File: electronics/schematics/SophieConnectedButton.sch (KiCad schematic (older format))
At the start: 13 parts, among them SW1 BT1, SW2 BT2, SW3 BT3, SW4 BT4

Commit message: Version semiminiature. Fin de journée 14octo2016
Inversion des serials 1 et 2
Modification de la patte Reset du module
Alignement de toutes les variables
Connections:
- wire segments 49 -> 52
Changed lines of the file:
@@
 	8050 3350 8050 3500
 Wire Wire Line
-	9300 2450 9300 3950
+	9300 2450 9300 4100
 Wire Wire Line
 	9300 3200 9050 3200
-Wire Wire Line
-	9300 3950 7850 3950
 Wire Wire Line
 	5950 3500 6050 3500
 Wire Wire Line
 	6050 3650 6200 3650
-Wire Wire Line
-	5950 3800 6200 3800
 Wire Wire Line
 	6050 3500 6050 3650
@@
 	1    0    0    -1
 $EndComp
-Wire Wire Line
-	5350 3250 5350 3800
 $Comp
 L +3.3V #PWR?
@@
 Wire Wire Line
 	8650 3500 8650 3650
-Wire Wire Line
-	8650 3650 8850 3650
 Wire Wire Line
 	4000 1950 4400 1950
@@
 $EndComp
 Wire Wire Line
-	6200 3350 6100 3350
-Wire Wire Line
-	6100 3350 6100 1500
-Wire Wire Line
-	6100 1500 2400 1500
-Wire Wire Line
 	2400 1500 2400 2050
 Wire Wire Line
@@
 Wire Wire Line
 	4900 2850 4900 3000
+Wire Wire Line
+	9300 4100 7850 4100
+Connection ~ 7850 4100
+Wire Wire Line
+	8850 3950 7950 3950
+Wire Wire Line
+	5350 3250 5350 3800
+Connection ~ 5350 3250
+Connection ~ 3400 2200
+Wire Wire Line
+	7950 3950 7950 3800
+Wire Wire Line
+	7950 3800 7850 3800
+Wire Wire Line
+	7850 3500 7950 3500
+Wire Wire Line
+	2400 1500 7950 1500
+Wire Wire Line
+	7950 1500 7950 3500
+Connection ~ 5350 3500
+Wire Wire Line
+	6200 3800 5950 3800
+Wire Wire Line
+	7850 3650 8850 3650
+Connection ~ 8650 3650
 $EndSCHEMATC

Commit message: Tests intermediaires
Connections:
- net labels added: +BATT
- wire segments 52 -> 53
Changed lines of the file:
@@
 	1    0    0    -1
 $EndComp
-Wire Wire Line
-	4000 4250 4000 4400
-Wire Wire Line
-	7850 3950 7850 4150
 $Comp
 L SW_PUSH SW3
@@
 	1    0    0    -1
 $EndComp
-Wire Wire Line
-	7850 3200 8150 3200
-Wire Wire Line
-	8450 3200 8650 3200
-Wire Wire Line
-	7850 3350 8050 3350
-Wire Wire Line
-	8050 3350 8050 3500
-Wire Wire Line
-	9300 2450 9300 4100
-Wire Wire Line
-	9300 3200 9050 3200
-Wire Wire Line
-	5950 3500 6050 3500
-Wire Wire Line
-	6050 3650 6200 3650
-Wire Wire Line
-	6050 3500 6050 3650
-Wire Wire Line
-	5950 3250 6150 3250
-Wire Wire Line
-	6150 3250 6150 3500
-Wire Wire Line
-	6150 3500 6200 3500
-Wire Wire Line
-	5900 2850 6000 2850
-Wire Wire Line
-	6000 2850 6000 3200
-Wire Wire Line
-	6000 3200 6200 3200
-Wire Wire Line
-	5400 2850 5600 2850
 $Comp
 L +3.3V #PWR?
@@
 	1    0    0    -1
 $EndComp
-Wire Wire Line
-	8650 3500 8650 3650
-Wire Wire Line
-	4000 1950 4400 1950
-Wire Wire Line
-	4400 1850 4400 2000
-Wire Wire Line
-	4400 1850 4000 1850
 $Comp
 L GND #PWR?
@@
 	1    0    0    -1
 $EndComp
-Wire Wire Line
-	7850 3050 8700 3050
-Wire Wire Line
-	8700 3050 8700 2900
-Wire Wire Line
-	7850 2900 8450 2900
-Wire Wire Line
-	8450 2900 8450 2800
-Wire Wire Line
-	8450 2800 8700 2800
-Wire Wire Line
-	8700 2700 8700 2450
-Wire Wire Line
-	8700 2450 9300 2450
-Connection ~ 9300 3200
 $Comp
 L GND #PWR?
@@
 	1    0    0    -1
 $EndComp
-Wire Wire Line
-	2400 1500 2400 2050
-Wire Wire Line
-	6650 2250 6650 1950
-Wire Wire Line
-	6650 1950 4900 1950
-Wire Wire Line
-	4900 1950 4900 2550
-Wire Wire Line
-	4900 2550 4000 2550
-Wire Wire Line
-	2400 2550 2300 2550
-Wire Wire Line
-	2300 2550 2300 1400
-Wire Wire Line
-	2300 1400 6800 1400
-Wire Wire Line
-	6800 1400 6800 2250
 $Comp
 L CONN_01X02 P?
@@
 	-1   0    0    -1
 $EndComp
+$Comp
+L +3.3V #PWR?
+U 1 1 580109B9
+P 4400 1750
+F 0 "#PWR?" H 4400 1600 50  0001 C CNN
+F 1 "+3.3V" H 4400 1890 50  0000 C CNN
+F 2 "" H 4400 1750 50  0000 C CNN
+F 3 "" H 4400 1750 50  0000 C CNN
+	1    4400 1750
+	1    0    0    -1
+$EndComp
+Wire Wire Line
+	4000 4250 4000 4400
+Wire Wire Line
+	7850 3950 7850 4150
+Wire Wire Line
+	7850 3200 8150 3200
+Wire Wire Line
+	8450 3200 8650 3200
+Wire Wire Line
+	7850 3350 8050 3350
+Wire Wire Line
+	8050 3350 8050 3500
+Wire Wire Line
+	9300 2450 9300 4100
+Wire Wire Line
+	9300 3200 9050 3200
+Wire Wire Line
+	5950 3500 6050 3500
+Wire Wire Line
+	6050 3650 6200 3650
+Wire Wire Line
+	6050 3500 6050 3650
+Wire Wire Line
+	5950 3250 6150 3250
+Wire Wire Line
+	6150 3250 6150 3500
+Wire Wire Line
+	6150 3500 6200 3500
+Wire Wire Line
+	5900 2850 6000 2850
+Wire Wire Line
+	6000 2850 6000 3200
+Wire Wire Line
+	6000 3200 6200 3200
+Wire Wire Line
+	5400 2850 5600 2850
+Wire Wire Line
+	8650 3500 8650 3650
+Wire Wire Line
+	4000 1950 4400 1950
+Wire Wire Line
+	4400 1750 4400 2000
+Wire Wire Line
+	4400 1850 4000 1850
+Wire Wire Line
+	7850 3050 8700 3050
+Wire Wire Line
+	8700 3050 8700 2900
+Wire Wire Line
+	7850 2900 8450 2900
+Wire Wire Line
+	8450 2900 8450 2800
+Wire Wire Line
+	8450 2800 8700 2800
+Wire Wire Line
+	8700 2700 8700 2450
+Wire Wire Line
+	8700 2450 9300 2450
+Connection ~ 9300 3200
+Wire Wire Line
+	2400 1500 2400 2050
+Wire Wire Line
+	6650 2250 6650 1950
+Wire Wire Line
+	6650 1950 4900 1950
+Wire Wire Line
+	4900 1950 4900 2550
+Wire Wire Line
+	4900 2550 4000 2550
+Wire Wire Line
+	2400 2550 2300 2550
+Wire Wire Line
+	2300 2550 2300 1400
+Wire Wire Line
+	2300 1400 6800 1400
+Wire Wire Line
+	6800 1400 6800 2250
 Wire Wire Line
 	2050 2150 2400 2150
@@
 Connection ~ 7850 4100
 Wire Wire Line
-	8850 3950 7950 3950
+	7950 3950 9050 3950
 Wire Wire Line
 	5350 3250 5350 3800
 Connection ~ 5350 3250
-Connection ~ 3400 2200
 Wire Wire Line
 	7950 3950 7950 3800
@@
 	7850 3650 8850 3650
 Connection ~ 8650 3650
+Connection ~ 4400 1850
+Connection ~ 4400 1950
+$Comp
+L +BATT #PWR?
+U 1 1 580117AC
+P 9050 3850
+F 0 "#PWR?" H 9050 3700 50  0001 C CNN
+F 1 "+BATT" H 9050 3990 50  0000 C CNN
+F 2 "" H 9050 3850 50  0000 C CNN
+F 3 "" H 9050 3850 50  0000 C CNN
+	1    9050 3850
+	1    0    0    -1
+$EndComp
+Wire Wire Line
+	9050 3950 9050 3850
 $EndSCHEMATC

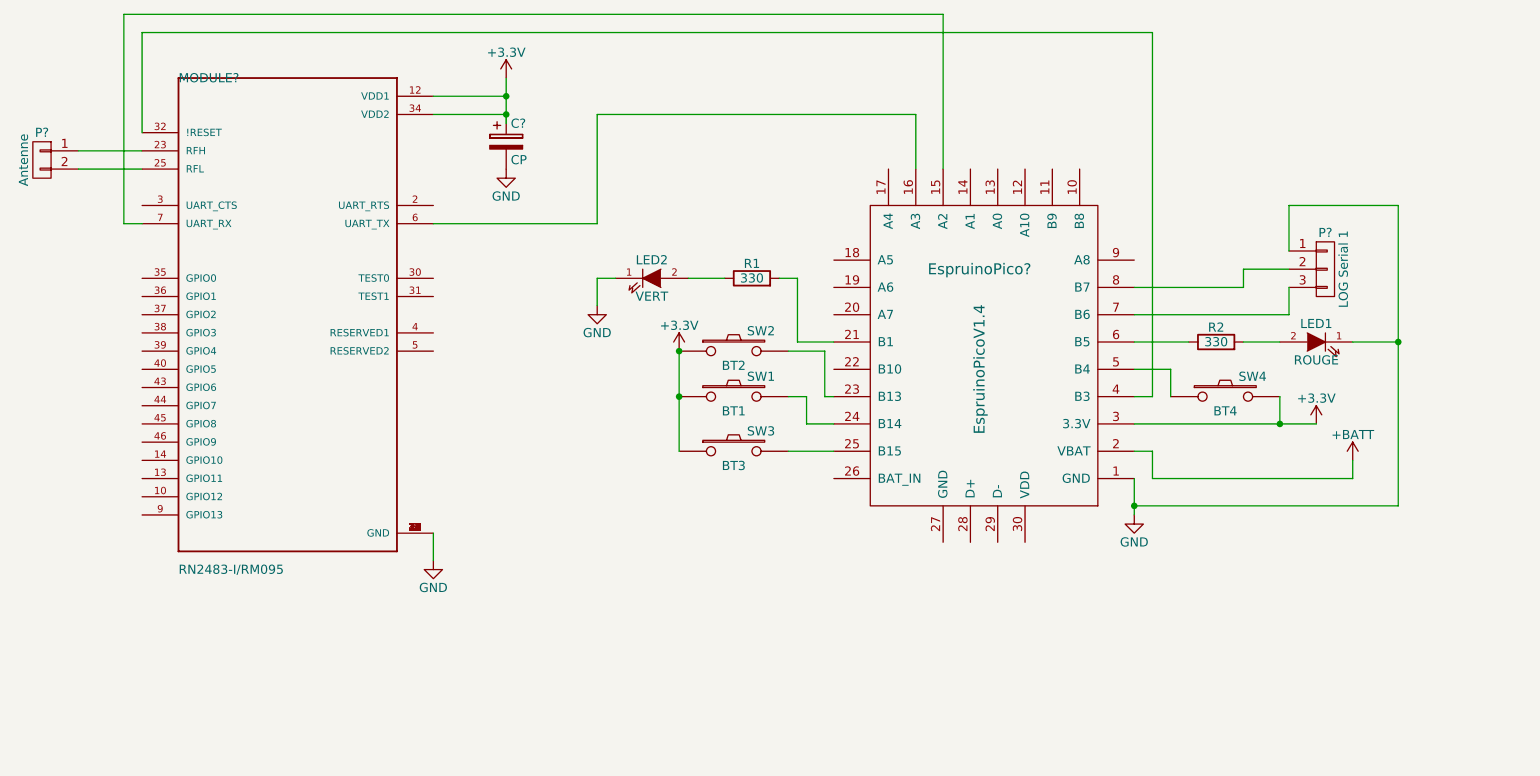
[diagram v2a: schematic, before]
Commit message: Forçage de la console sur USB
Correction forçant la console sur l'USB, ne polluant plus Serial1.
Divers nettoyages.
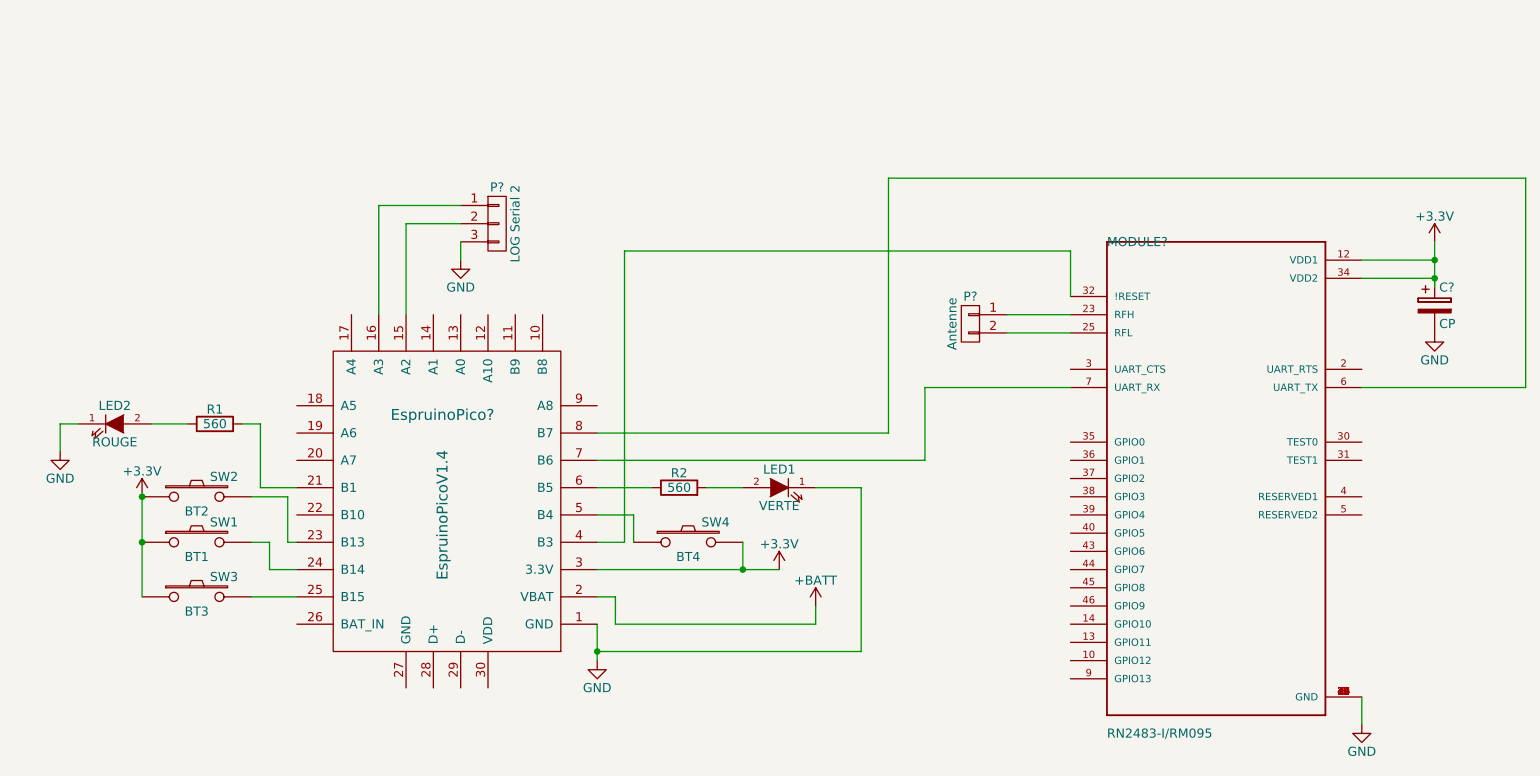
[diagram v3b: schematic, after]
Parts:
- LED1: value ROUGE -> VERTE
- LED2: value VERT -> ROUGE
- P?: value LOG Serial 1 -> LOG Serial 2
- R1, R2: value 330 -> 560
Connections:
- net GND: now also P?.3 (P3); no longer P?.1 (P1)
- net at MODULE?.6 (UART_TX): now also EspruinoPico?.8 (B7); no longer EspruinoPico?.16 (A3)
- net at MODULE?.7 (UART_RX): now also EspruinoPico?.7 (B6); no longer EspruinoPico?.15 (A2)
- net at P?.2 (P2): now also EspruinoPico?.15 (A2); no longer EspruinoPico?.8 (B7)
- new net: EspruinoPico?.16 (A3), P?.1 (P1)
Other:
- moved on the sheet: C?, EspruinoPico?, LED1, LED2, MODULE?, P?, R1, R2, SW1, SW2, SW3, SW4
